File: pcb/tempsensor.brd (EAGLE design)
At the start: 88.6 x 20.3 mm, 18 parts, among them Q1 DS18X20TO92, Q2 DS18X20SO-8

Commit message: Update PCB
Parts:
- moved R6 1.91 mm to (30.5, 17.1), turned to 90 degrees
- moved R4 1.27 mm to (48.9, 8.89)
- moved R3 0.63 mm to (49.5, 13.3), turned to 270 degrees
- moved R5 0.63 mm to (33.0, 17.1)
- renumbered U$3 to U1
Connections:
- net RX_5V: now also R1.1, T1.2; no longer R5.2
- net TX: now also R3.1, T1.1; no longer R1.1, T1.2
- net TX_5V: now also R5.2; no longer R3.1, T1.1
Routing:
- net VCC: track 90.8 -> 79.2 mm, vias 3 -> 1
- net TX_5V: track 14.5 -> 8.65 mm, vias 0 -> 1
- net RX_5V: track 4.47 -> 9.96 mm
- net GND: track 62.3 -> 58.9 mm, vias 3 -> 4
- net +5V: track 9.19 -> 5.93 mm, vias 1 -> 0
- net TX: track 26.7 -> 24.1 mm
- net RX: track 35.6 -> 34.3 mm
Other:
- board text added: "ESP8166-Temperatursensor v 1.0 Thomas Zimmermann July 2015"

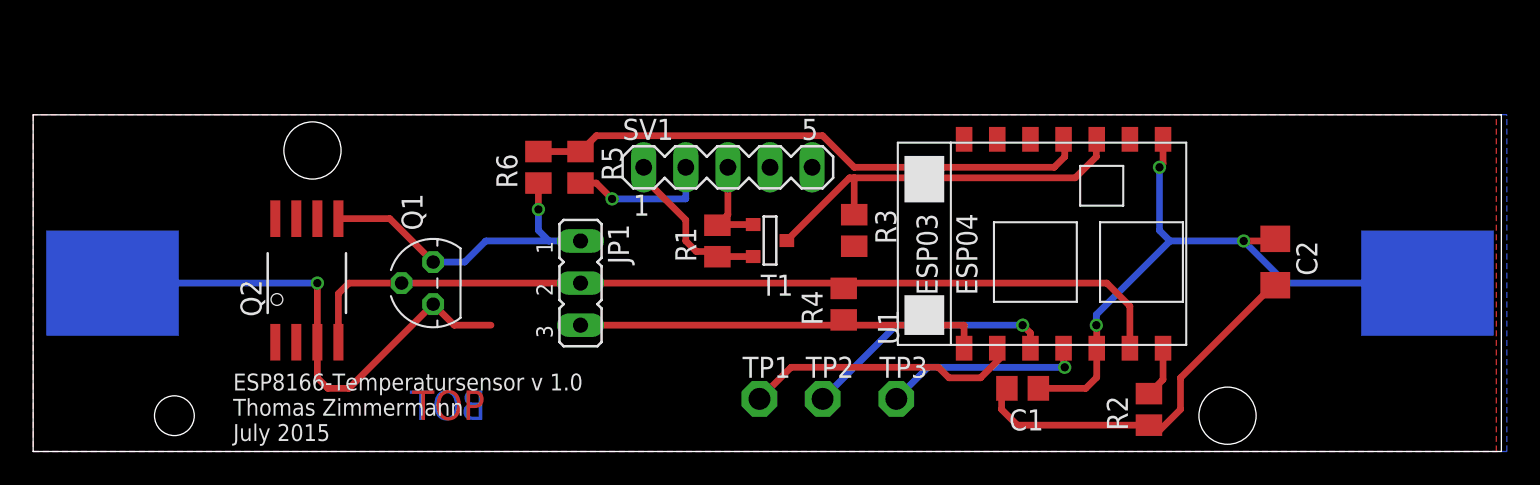
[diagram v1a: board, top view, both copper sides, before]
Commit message: Update PCB: Add lipo charging circuit based on mcp73831 and Reset und Program buttons
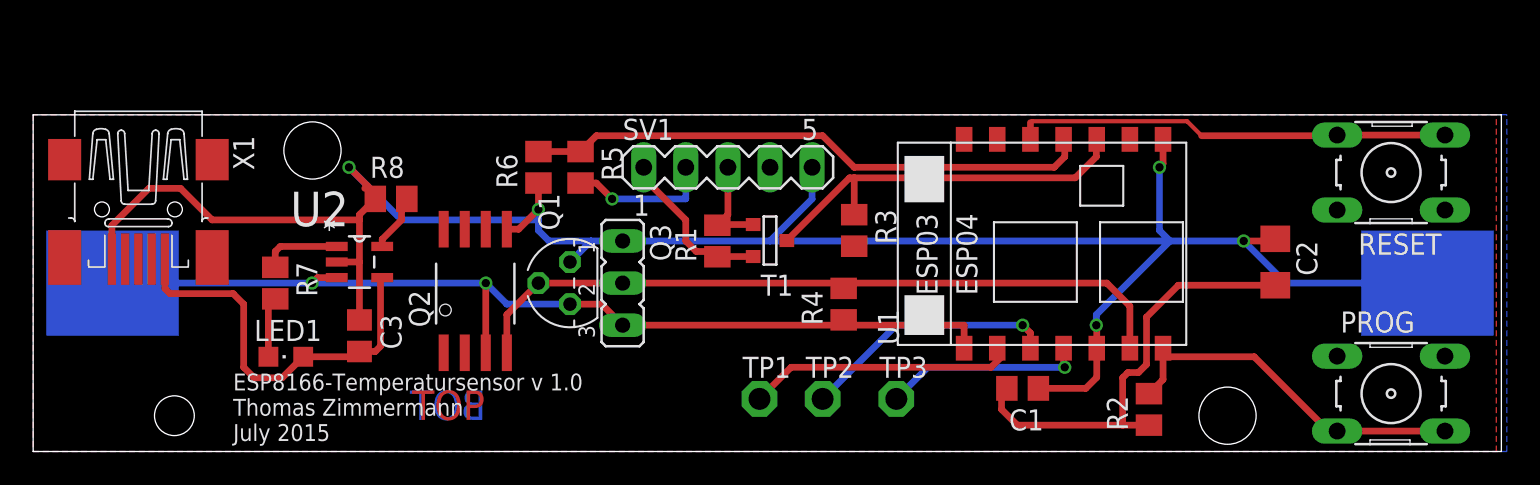
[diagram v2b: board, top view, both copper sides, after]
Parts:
- removed JP1: (no value), jumper:JP2
- added C3: 4u7, resistor:C0805
- added LED1: (no value), led:CHIPLED_0805
- added PROG, RESET: (no value), switch-omron:B3F-10XX
- added Q3: (no value), jumper:JP2
- added R7: 470R, resistor:M0805
- added R8: 2k, resistor:M0805
- added U2: MCP73831T-2DCI/OT, Microchip-MCP73831T-2DCI_OT:SOT95P270X145-5N
- added X1: MINI-USB-32005-201, con-cypressindustries:32005-201
- moved Q2 10.2 mm to (26.7, 9.53)
- moved Q1 8.25 mm to (32.4, 10.2)
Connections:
- new net N$5: LED1.C, R7.2
- new net N$6: R8.2, U2.5
- new net PROG: PROG.3, PROG.4, R2.2, U1.GPIO0
- new net RST: RESET.3, RESET.4, U1.GPIO18
- new net V+: C3.2, LED1.A, U2.4, X1.1
- net DQ: now also Q3.2; no longer JP1.2
- net GND: now also C3.1, PROG.1, PROG.2, Q3.1, R8.1, RESET.1, RESET.2, U2.2, X1.5; no longer JP1.1
- net N$1: now also R7.1, U2.1; no longer R2.2, U1.GPIO0
- net VCC: now also Q3.3, U2.3; no longer JP1.3
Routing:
- net GND: track 58.9 -> 133.1 mm, vias 4 -> 5
- net RST: track 0.00 -> 26.4 mm
- net V+: track 0.00 -> 24.2 mm
- net PROG: track 0.00 -> 21.9 mm
- net DQ: track 54.4 -> 44.1 mm
- net VCC: track 79.2 -> 87.0 mm, vias 1 -> 2
- net N$5: track 0.00 -> 3.67 mm
- net N$6: track 0.00 -> 3.48 mm
- net N$1: track 3.09 -> 4.79 mm
- net N$4: track 17.1 -> 16.6 mm

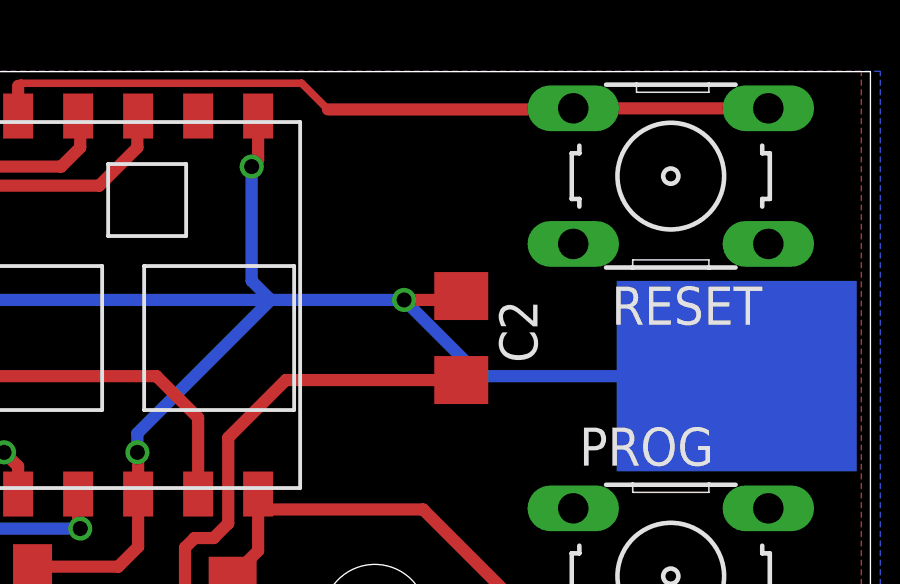
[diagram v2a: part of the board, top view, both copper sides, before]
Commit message: PCB: add optional pullup resistor for RESET pin, and additional 100u cap for power
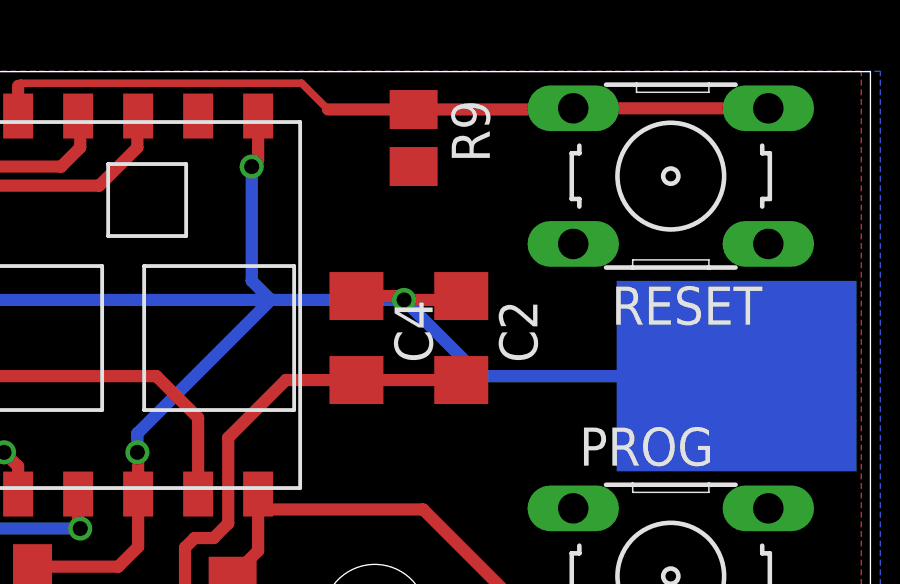
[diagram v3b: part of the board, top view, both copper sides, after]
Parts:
- added C4: 100u, resistor:C1206
- added R9: 4K7, resistor:M0805
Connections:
- net GND: now also C4.1
- net RST: now also R9.1
- net VCC: now also C4.2, R9.2
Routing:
- net GND: track 133.1 -> 134.7 mm
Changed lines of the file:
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@@
 <attribute name="OC_FARNELL" value="unknown" x="6.35" y="14.605" size="1.778" layer="27" rot="R270" display="off"/>
 </element>
+<element name="R9" library="resistor" package="M0805" value="4K7" x="73.3425" y="18.0975" rot="R270"/>
+<element name="C4" library="resistor" package="C1206" value="100u" x="71.4375" y="11.43" rot="R270"/>
 </elements>
 <signals>
@@
 <wire x1="17.1577" y1="10.4902" x2="16.8275" y2="10.16" width="0.4064" layer="1"/>
 <via x="16.8275" y="10.16" extent="1-16" drill="0.5"/>
+<contactref element="R9" pad="2"/>
+<contactref element="C4" pad="2"/>
 </signal>
 <signal name="GND">
@@
 <wire x1="8.89" y1="15.875" x2="10.795" y2="13.97" width="0.4064" layer="1"/>
 <wire x1="10.795" y1="13.97" x2="19.685" y2="13.97" width="0.4064" layer="1"/>
+<contactref element="C4" pad="1"/>
+<wire x1="71.4375" y1="12.83" x2="72.895" y2="12.83" width="0.4064" layer="1"/>
+<wire x1="72.895" y1="12.83" x2="73.025" y2="12.7" width="0.4064" layer="1"/>
 </signal>
 <signal name="RX">
@@
 <wire x1="60.245625" y1="19.923125" x2="69.611875" y2="19.923125" width="0.254" layer="1"/>
 <wire x1="69.611875" y1="19.923125" x2="70.485" y2="19.05" width="0.254" layer="1"/>
-<wire x1="70.485" y1="19.05" x2="78.6257" y2="19.05" width="0.4064" layer="1"/>
+<wire x1="70.485" y1="19.05" x2="73.3425" y2="19.05" width="0.4064" layer="1"/>
+<wire x1="73.3425" y1="19.05" x2="78.6257" y2="19.05" width="0.4064" layer="1"/>
 <wire x1="78.6257" y1="19.05" x2="78.6638" y2="19.0881" width="0.4064" layer="1"/>
+<contactref element="R9" pad="1"/>
+<wire x1="73.3425" y1="19.0475" x2="73.3425" y2="19.05" width="0.4064" layer="1"/>
 </signal>
 <signal name="N$1">

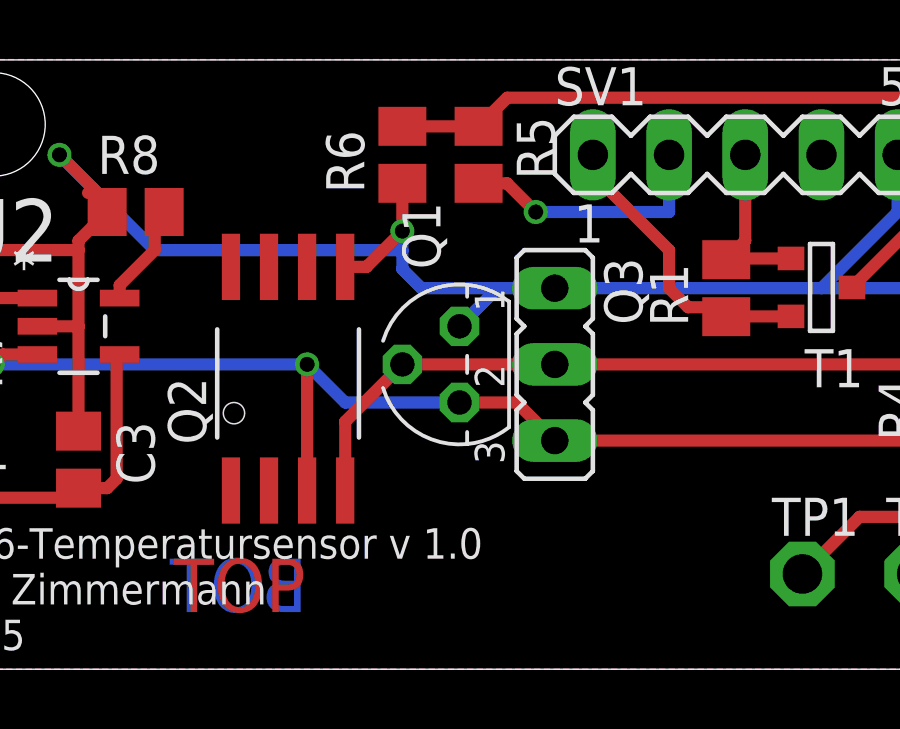
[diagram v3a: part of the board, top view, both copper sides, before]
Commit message: Fix Footprint for DS18B20, VCC and GND were swaped
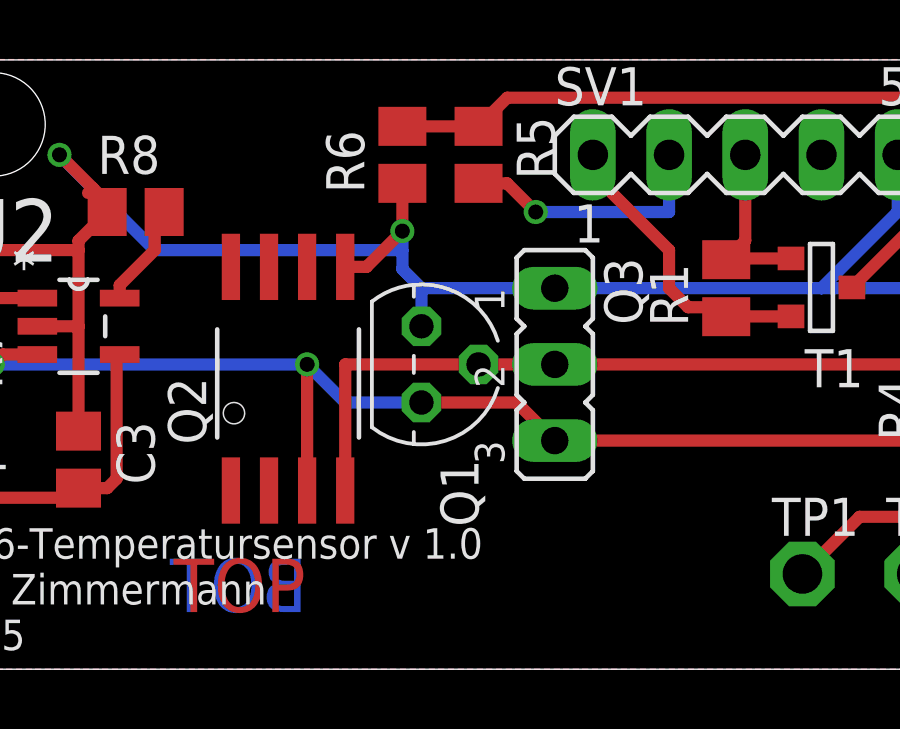
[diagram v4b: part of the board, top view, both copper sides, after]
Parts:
- moved Q1 1.27 mm to (31.1, 10.2), turned to 270 degrees
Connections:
- net GND: now also Q1.3; no longer Q1.1
- net VCC: now also Q1.1; no longer Q1.3
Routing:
- net DQ: track 44.1 -> 45.2 mm
- net GND: track 134.7 -> 134.2 mm
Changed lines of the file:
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@@
 <element name="C2" library="resistor" package="C1206" value="100u" x="74.93" y="11.43" rot="R270"/>
 <element name="Q3" library="jumper" package="JP2" value="" x="35.56" y="10.16" rot="R270"/>
-<element name="Q1" library="ds18x20-board" package="TO92" value="DS18X20TO92" x="32.385" y="10.16" rot="R90"/>
+<element name="Q1" library="ds18x20-board" package="TO92" value="DS18X20TO92" x="31.115" y="10.16" rot="R270"/>
 <element name="Q2" library="ds18x20-board" package="SO08WIDE" value="DS18X20SO-8" x="26.67" y="9.525"/>
 <element name="R2" library="resistor" package="M0805" value="4K7" x="67.31" y="2.54" rot="R90"/>
@@
 <contactref element="C2" pad="2"/>
 <contactref element="R2" pad="1"/>
-<contactref element="Q1" pad="3"/>
+<contactref element="Q1" pad="1"/>
 <contactref element="Q2" pad="3"/>
 <contactref element="Q3" pad="3"/>
@@
 <wire x1="65.7225" y1="4.445" x2="65.7225" y2="1.59" width="0.4064" layer="1"/>
 <contactref element="U2" pad="3"/>
-<wire x1="32.385" y1="8.89" x2="34.29" y2="8.89" width="0.4064" layer="1"/>
+<wire x1="31.115" y1="8.89" x2="34.29" y2="8.89" width="0.4064" layer="1"/>
 <wire x1="34.29" y1="8.89" x2="35.56" y2="7.62" width="0.4064" layer="1"/>
-<wire x1="32.385" y1="8.89" x2="28.575" y2="8.89" width="0.4064" layer="16"/>
+<wire x1="31.115" y1="8.89" x2="28.575" y2="8.89" width="0.4064" layer="16"/>
 <wire x1="28.575" y1="8.89" x2="27.305" y2="10.16" width="0.4064" layer="16"/>
 <wire x1="18.3134" y1="10.4902" x2="17.1577" y2="10.4902" width="0.4064" layer="1"/>
@@
 <contactref element="C2" pad="1"/>
 <contactref element="SV1" pad="5"/>
-<contactref element="Q1" pad="1"/>
+<contactref element="Q1" pad="3"/>
 <contactref element="Q2" pad="5"/>
 <contactref element="Q3" pad="1"/>
@@
 <vertex x="88.9" y="20.32"/>
 </polygon>
-<wire x1="35.56" y1="12.7" x2="33.655" y2="12.7" width="0.4064" layer="16"/>
-<wire x1="31.115" y1="12.7" x2="33.655" y2="12.7" width="0.4064" layer="16"/>
-<wire x1="33.655" y1="12.7" x2="32.385" y2="11.43" width="0.4064" layer="16"/>
+<wire x1="35.56" y1="12.7" x2="31.115" y2="12.7" width="0.4064" layer="16"/>
+<wire x1="31.115" y1="12.7" x2="31.115" y2="11.43" width="0.4064" layer="16"/>
 <wire x1="68.16" y1="18.83" x2="68.16" y2="17.36" width="0.4064" layer="1"/>
 <wire x1="68.16" y1="17.36" x2="67.945" y2="17.145" width="0.4064" layer="1"/>
@@
 <wire x1="64.77" y1="10.16" x2="66.16" y2="8.77" width="0.4064" layer="1"/>
 <wire x1="66.16" y1="6.23" x2="66.16" y2="8.77" width="0.4064" layer="1"/>
-<wire x1="30.48" y1="10.16" x2="35.56" y2="10.16" width="0.4064" layer="1"/>
+<wire x1="33.02" y1="10.16" x2="35.56" y2="10.16" width="0.4064" layer="1"/>
 <wire x1="64.77" y1="10.16" x2="48.895" y2="10.16" width="0.4064" layer="1"/>
 <wire x1="48.895" y1="10.16" x2="35.56" y2="10.16" width="0.4064" layer="1"/>
 <wire x1="48.895" y1="9.84" x2="48.895" y2="10.16" width="0.4064" layer="1"/>
-<wire x1="30.48" y1="10.16" x2="28.575" y2="8.255" width="0.4064" layer="1"/>
-<wire x1="28.575" y1="8.255" x2="28.575" y2="5.9563" width="0.4064" layer="1"/>
+<wire x1="33.02" y1="10.16" x2="28.575" y2="10.16" width="0.4064" layer="1"/>
+<wire x1="28.575" y1="10.16" x2="28.575" y2="5.9563" width="0.4064" layer="1"/>
 </signal>
 <signal name="PROG">

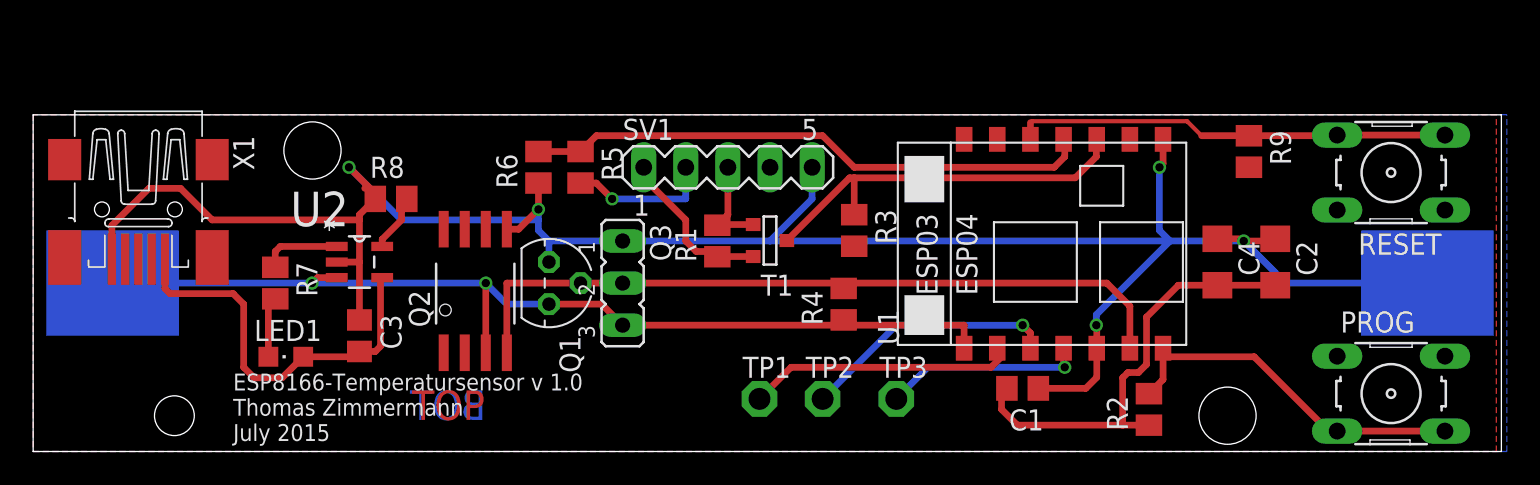
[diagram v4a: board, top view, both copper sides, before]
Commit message: PCB: increase size of batterholder pads and rotate esp-03 so that it's antenna is no longer shielded
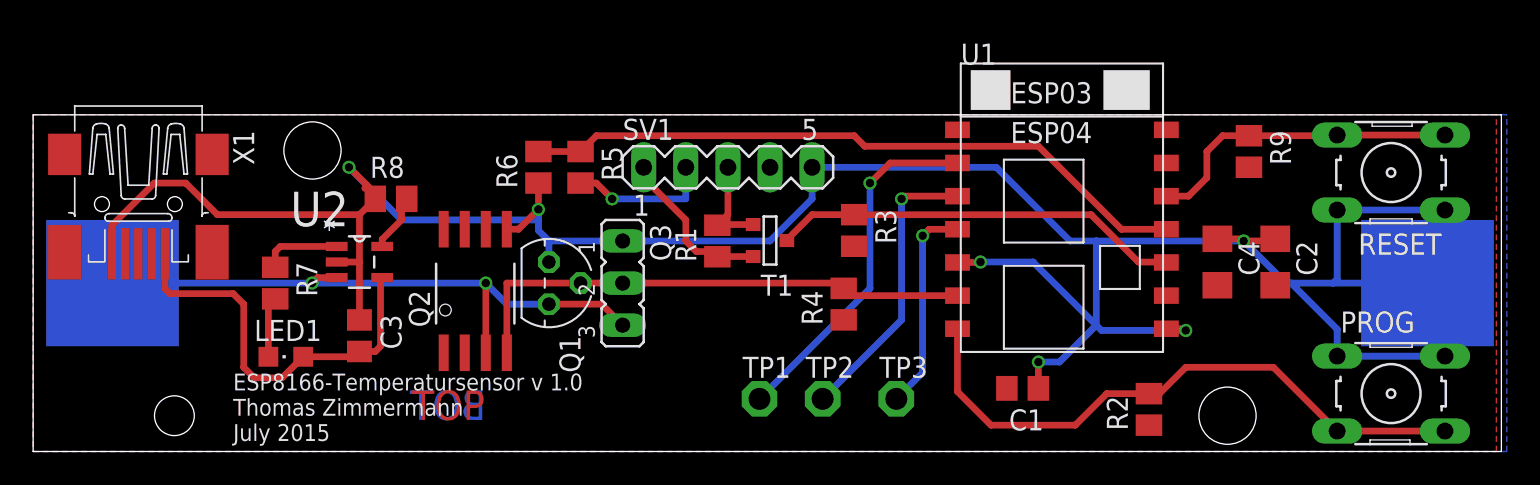
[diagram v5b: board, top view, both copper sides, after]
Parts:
- moved U1 3.18 mm to (61.0, 14.6), turned to 0 degrees
- moved X1 0.32 mm to (6.35, 14.9)
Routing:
- net VCC: track 87.0 -> 38.2 mm
- net GND: track 134.2 -> 163.8 mm, vias 5 -> 6
- net PROG: track 21.9 -> 37.1 mm
- net DQ: track 45.2 -> 31.7 mm
- net RST: track 26.4 -> 19.3 mm
- net RX: track 34.3 -> 40.6 mm
- net N$4: track 16.6 -> 21.6 mm, vias 0 -> 1
- net N$3: track 15.5 -> 17.5 mm
- net TX: track 24.1 -> 24.8 mm
- net N$2: track 12.1 -> 12.8 mm

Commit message: PCB: rename testpoints, add points for VCC and GND, add RP-SMA connector for external antenna
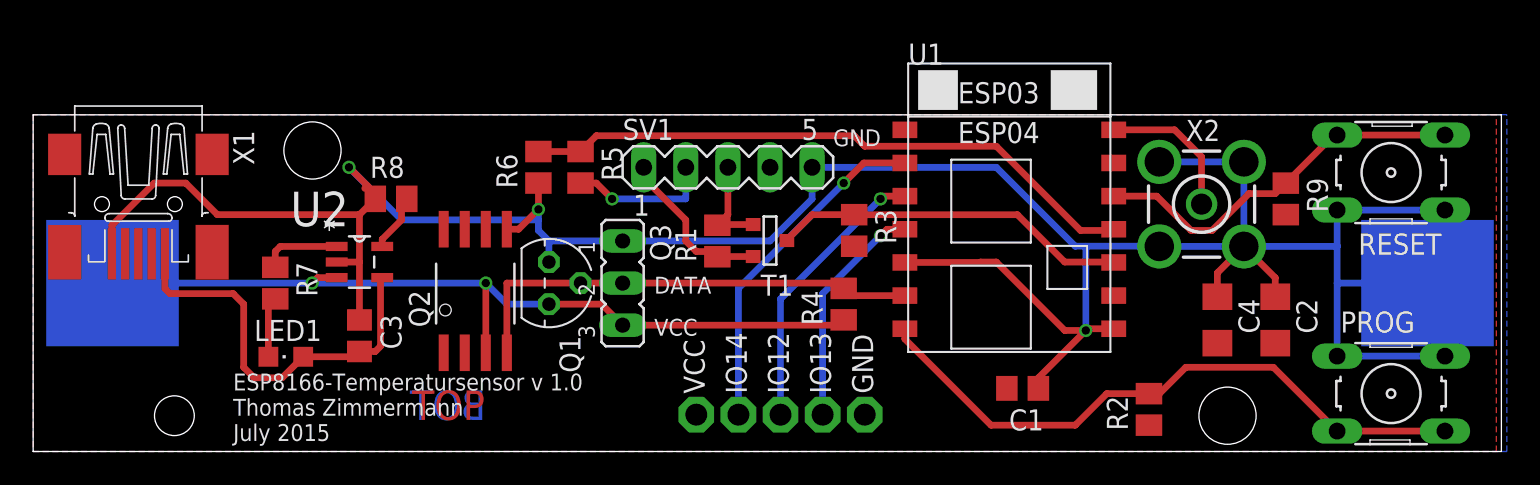
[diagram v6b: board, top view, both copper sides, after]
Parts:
- removed TP1, TP2, TP3: TPPAD1-13, testpad:P1-13
- added GND, IO12, IO13, IO14, VCC: TPPAD1-13, testpad:P1-13
- added X2: BU-SMA-V, con-coax:BU-SMA-V
- moved R9 3.62 mm to (75.6, 15.2)
- moved C2 3.49 mm to (74.9, 7.94)
- moved C4 3.49 mm to (71.4, 7.94)
- moved U1 3.18 mm to (57.8, 14.6)
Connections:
- new net N$7: U1.ANT, X2.1
- net GND: now also GND.TP, X2.2, X2.3, X2.4, X2.5
- net N$2: now also IO13.TP; no longer TP3.TP
- net N$3: now also IO12.TP; no longer TP2.TP
- net N$4: now also IO14.TP; no longer TP1.TP
- net VCC: now also VCC.TP
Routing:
- net VCC: track 38.2 -> 51.6 mm
- net N$7: track 0.00 -> 8.83 mm
- net GND: track 163.8 -> 172.1 mm, vias 6 -> 3
- net RST: track 19.3 -> 23.2 mm
- net TX: track 24.8 -> 21.7 mm
- net DQ: track 31.7 -> 28.5 mm
- net RX: track 40.6 -> 37.5 mm
- net PROG: track 37.1 -> 38.4 mm
- net N$2: track 12.8 -> 13.9 mm
- net N$4: track 21.6 -> 20.8 mm
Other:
- board text added: "DATA"
- board text added: "GND"
- board text added: "VCC"
